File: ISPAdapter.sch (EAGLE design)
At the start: 8 parts, among them U1 SWITCH_IC_QUAD74LVC4066

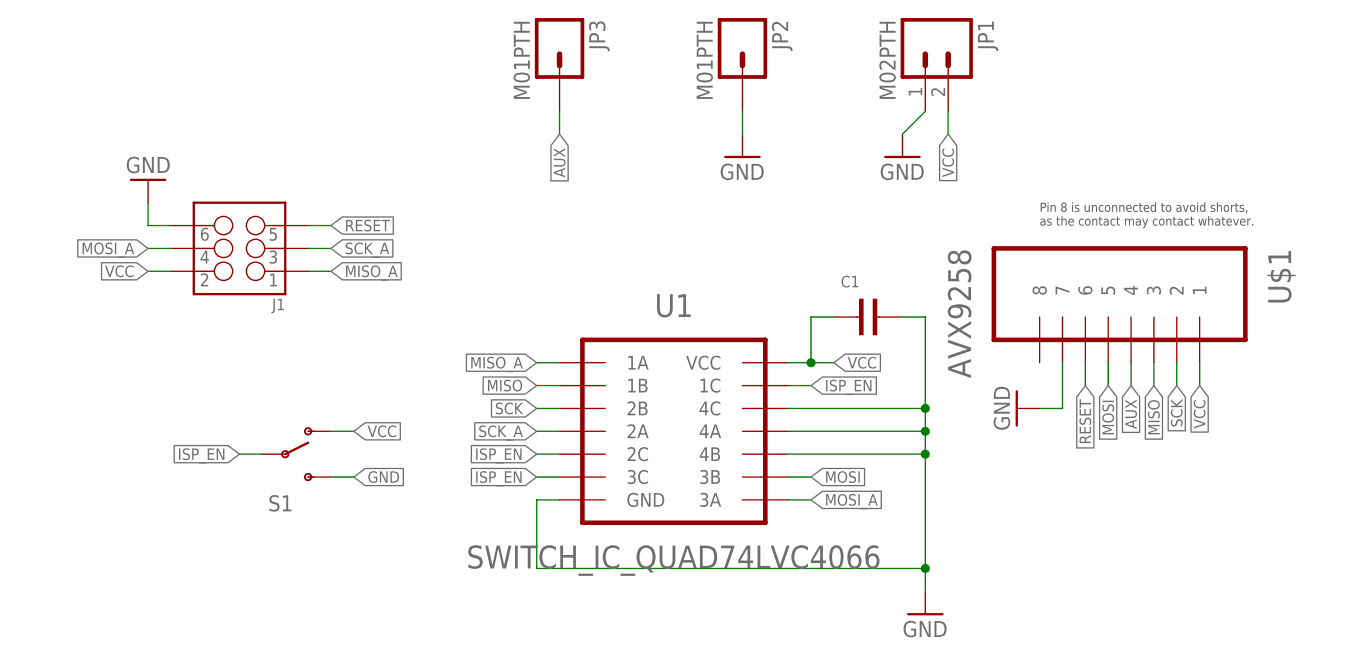
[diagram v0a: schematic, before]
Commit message: Switch IC fitting
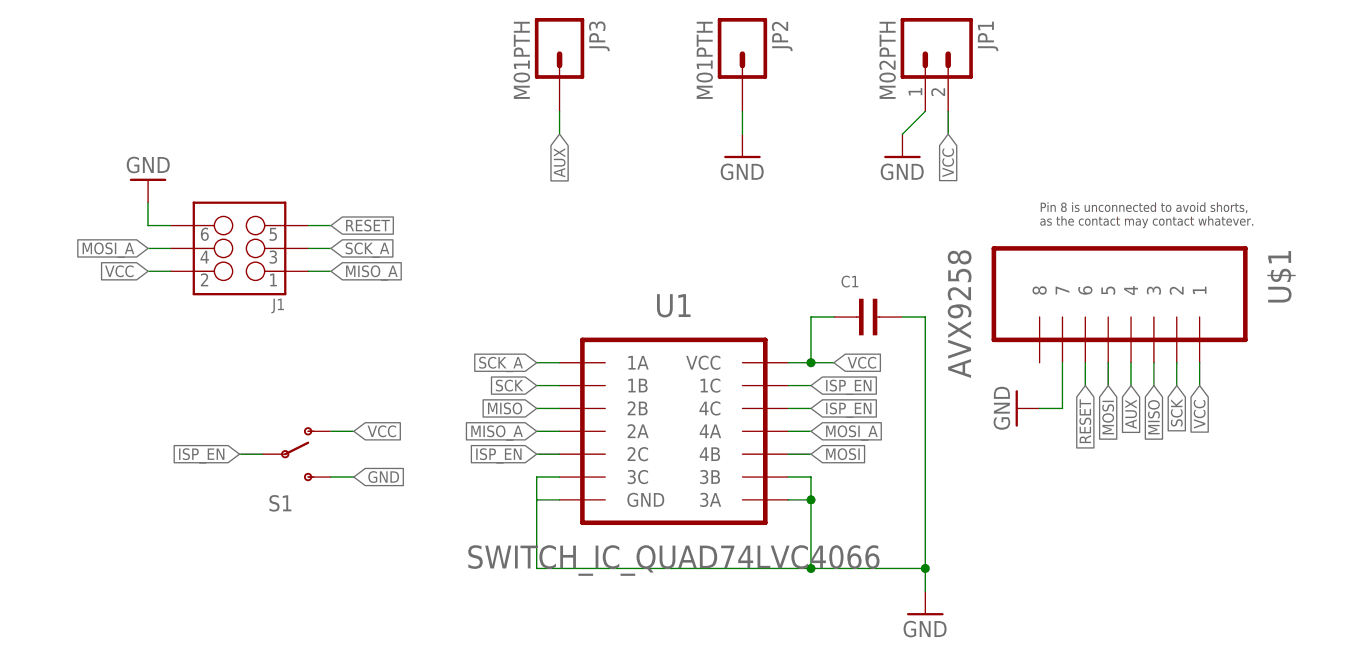
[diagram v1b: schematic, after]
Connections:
- net DGND: now also U1.3A, U1.3B, U1.3C; no longer U1.4A, U1.4B, U1.4C
- net ISP_EN: now also U1.4C; no longer U1.3C
- net MISO: now also U1.2B; no longer U1.1B
- net MISO_A: now also U1.2A; no longer U1.1A
- net MOSI: now also U1.4B; no longer U1.3B
- net MOSI_A: now also U1.4A; no longer U1.3A
- net SCK: now also U1.1B; no longer U1.2B
- net SCK_A: now also U1.1A; no longer U1.2A
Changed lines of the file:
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@@
 </segment>
 <segment>
-<pinref part="U1" gate="G$1" pin="3B"/>
-<wire x1="71.12" y1="43.18" x2="73.66" y2="43.18" width="0.1524" layer="91"/>
-<label x="73.66" y="43.18" size="1.27" layer="95" xref="yes"/>
+<pinref part="U1" gate="G$1" pin="4B"/>
+<wire x1="71.12" y1="45.72" x2="73.66" y2="45.72" width="0.1524" layer="91"/>
+<label x="73.66" y="45.72" size="1.27" layer="95" xref="yes"/>
 </segment>
 </net>
@@
 <pinref part="U1" gate="G$1" pin="GND"/>
 <wire x1="45.72" y1="40.64" x2="43.18" y2="40.64" width="0.1524" layer="91"/>
+<pinref part="U1" gate="G$1" pin="3C"/>
+<wire x1="45.72" y1="43.18" x2="43.18" y2="43.18" width="0.1524" layer="91"/>
+<wire x1="43.18" y1="43.18" x2="43.18" y2="40.64" width="0.1524" layer="91"/>
 </segment>
 <segment>
 <pinref part="GND6" gate="1" pin="GND"/>
 <wire x1="43.18" y1="40.64" x2="43.18" y2="33.02" width="0.1524" layer="91"/>
-<pinref part="U1" gate="G$1" pin="4C"/>
-<wire x1="71.12" y1="50.8" x2="86.36" y2="50.8" width="0.1524" layer="91"/>
-<wire x1="86.36" y1="50.8" x2="86.36" y2="48.26" width="0.1524" layer="91"/>
-<pinref part="U1" gate="G$1" pin="4A"/>
-<wire x1="86.36" y1="48.26" x2="86.36" y2="45.72" width="0.1524" layer="91"/>
-<wire x1="86.36" y1="45.72" x2="86.36" y2="33.02" width="0.1524" layer="91"/>
 <wire x1="86.36" y1="33.02" x2="86.36" y2="30.48" width="0.1524" layer="91"/>
-<wire x1="71.12" y1="48.26" x2="86.36" y2="48.26" width="0.1524" layer="91"/>
-<junction x="86.36" y="48.26"/>
-<pinref part="U1" gate="G$1" pin="4B"/>
-<wire x1="71.12" y1="45.72" x2="86.36" y2="45.72" width="0.1524" layer="91"/>
-<junction x="86.36" y="45.72"/>
-<wire x1="43.18" y1="33.02" x2="86.36" y2="33.02" width="0.1524" layer="91"/>
+<wire x1="43.18" y1="33.02" x2="73.66" y2="33.02" width="0.1524" layer="91"/>
 <junction x="86.36" y="33.02"/>
 <pinref part="C1" gate="G$1" pin="2"/>
+<wire x1="73.66" y1="33.02" x2="86.36" y2="33.02" width="0.1524" layer="91"/>
 <wire x1="83.82" y1="60.96" x2="86.36" y2="60.96" width="0.1524" layer="91"/>
-<wire x1="86.36" y1="60.96" x2="86.36" y2="50.8" width="0.1524" layer="91"/>
-<junction x="86.36" y="50.8"/>
+<wire x1="86.36" y1="60.96" x2="86.36" y2="33.02" width="0.1524" layer="91"/>
+<pinref part="U1" gate="G$1" pin="3B"/>
+<wire x1="71.12" y1="43.18" x2="73.66" y2="43.18" width="0.1524" layer="91"/>
+<pinref part="U1" gate="G$1" pin="3A"/>
+<wire x1="71.12" y1="40.64" x2="73.66" y2="40.64" width="0.1524" layer="91"/>
+<wire x1="73.66" y1="43.18" x2="73.66" y2="40.64" width="0.1524" layer="91"/>
+<wire x1="73.66" y1="40.64" x2="73.66" y2="33.02" width="0.1524" layer="91"/>
+<junction x="73.66" y="40.64"/>
+<junction x="73.66" y="33.02"/>
 </segment>
 </net>
@@
 </segment>
 <segment>
-<pinref part="U1" gate="G$1" pin="1B"/>
-<wire x1="45.72" y1="53.34" x2="43.18" y2="53.34" width="0.1524" layer="91"/>
-<label x="43.18" y="53.34" size="1.27" layer="95" rot="R180" xref="yes"/>
+<pinref part="U1" gate="G$1" pin="2B"/>
+<wire x1="45.72" y1="50.8" x2="43.18" y2="50.8" width="0.1524" layer="91"/>
+<label x="43.18" y="50.8" size="1.27" layer="95" rot="R180" xref="yes"/>
 </segment>
 </net>
@@
 </segment>
 <segment>
-<pinref part="U1" gate="G$1" pin="2B"/>
-<wire x1="45.72" y1="50.8" x2="43.18" y2="50.8" width="0.1524" layer="91"/>
-<label x="43.18" y="50.8" size="1.27" layer="95" rot="R180" xref="yes"/>
+<pinref part="U1" gate="G$1" pin="1B"/>
+<wire x1="45.72" y1="53.34" x2="43.18" y2="53.34" width="0.1524" layer="91"/>
+<label x="43.18" y="53.34" size="1.27" layer="95" rot="R180" xref="yes"/>
 </segment>
 </net>
@@
 </segment>
 <segment>
-<pinref part="U1" gate="G$1" pin="3C"/>
-<wire x1="45.72" y1="43.18" x2="43.18" y2="43.18" width="0.1524" layer="91"/>
-<label x="43.18" y="43.18" size="1.27" layer="95" rot="R180" xref="yes"/>
-</segment>
-<segment>
 <pinref part="S1" gate="1" pin="P"/>
 <wire x1="12.7" y1="45.72" x2="10.16" y2="45.72" width="0.1524" layer="91"/>
 <label x="10.16" y="45.72" size="1.27" layer="95" rot="R180" xref="yes"/>
+</segment>
+<segment>
+<pinref part="U1" gate="G$1" pin="4C"/>
+<wire x1="71.12" y1="50.8" x2="73.66" y2="50.8" width="0.1524" layer="91"/>
+<label x="73.66" y="50.8" size="1.27" layer="95" xref="yes"/>
 </segment>
 </net>
@@
 </segment>
 <segment>
-<pinref part="U1" gate="G$1" pin="2A"/>
-<wire x1="45.72" y1="48.26" x2="43.18" y2="48.26" width="0.1524" layer="91"/>
-<label x="43.18" y="48.26" size="1.27" layer="95" rot="R180" xref="yes"/>
+<pinref part="U1" gate="G$1" pin="1A"/>
+<wire x1="45.72" y1="55.88" x2="43.18" y2="55.88" width="0.1524" layer="91"/>
+<label x="43.18" y="55.88" size="1.27" layer="95" rot="R180" xref="yes"/>
 </segment>
 </net>
@@
 </segment>
 <segment>
-<pinref part="U1" gate="G$1" pin="1A"/>
-<wire x1="45.72" y1="55.88" x2="43.18" y2="55.88" width="0.1524" layer="91"/>
-<label x="43.18" y="55.88" size="1.27" layer="95" rot="R180" xref="yes"/>
+<pinref part="U1" gate="G$1" pin="2A"/>
+<wire x1="45.72" y1="48.26" x2="43.18" y2="48.26" width="0.1524" layer="91"/>
+<label x="43.18" y="48.26" size="1.27" layer="95" rot="R180" xref="yes"/>
 </segment>
 </net>
@@
 </segment>
 <segment>
-<pinref part="U1" gate="G$1" pin="3A"/>
-<wire x1="71.12" y1="40.64" x2="73.66" y2="40.64" width="0.1524" layer="91"/>
-<label x="73.66" y="40.64" size="1.27" layer="95" xref="yes"/>
+<pinref part="U1" gate="G$1" pin="4A"/>
+<wire x1="71.12" y1="48.26" x2="73.66" y2="48.26" width="0.1524" layer="91"/>
+<label x="73.66" y="48.26" size="1.27" layer="95" xref="yes"/>
 </segment>
 </net>

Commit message: Tidy
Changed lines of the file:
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@@
 <instance part="GND3" gate="1" x="83.82" y="78.74"/>
 <instance part="U$1" gate="G$1" x="109.22" y="63.5" rot="R270"/>
-<instance part="GND4" gate="1" x="96.52" y="50.8" rot="R270"/>
+<instance part="GND4" gate="1" x="99.06" y="50.8"/>
 <instance part="JP2" gate="G$1" x="66.04" y="91.44" rot="R270"/>
 <instance part="GND1" gate="1" x="66.04" y="78.74"/>
@@
 <segment>
 <pinref part="GND4" gate="1" pin="GND"/>
-<wire x1="101.6" y1="50.8" x2="99.06" y2="50.8" width="0.1524" layer="91"/>
+<wire x1="101.6" y1="55.88" x2="99.06" y2="53.34" width="0.1524" layer="91"/>
 <pinref part="U$1" gate="G$1" pin="7"/>
-<wire x1="101.6" y1="50.8" x2="101.6" y2="55.88" width="0.1524" layer="91"/>
 </segment>
 <segment>

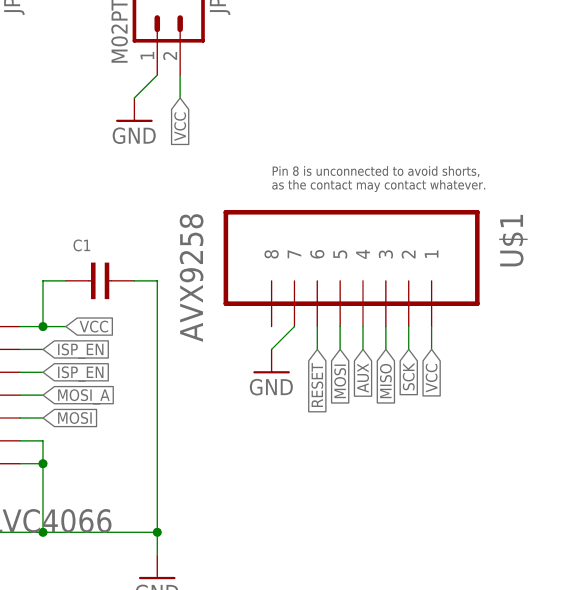
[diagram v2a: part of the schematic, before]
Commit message: Full connector mapping
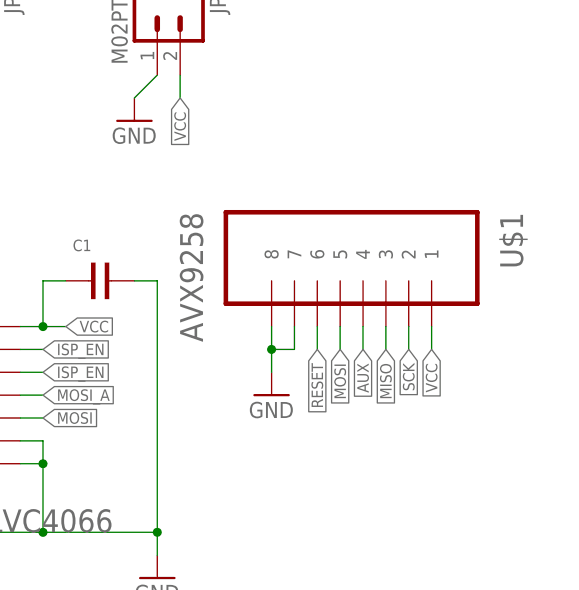
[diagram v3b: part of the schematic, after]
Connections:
- net DGND: now also U$1.8
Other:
- note removed: "Pin 8 is unconnected to avoid shorts, as the contact may contact whatever."
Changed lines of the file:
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@@
 <sheet>
 <plain>
-<text x="99.06" y="73.66" size="1.016" layer="97" align="top-left">Pin 8 is unconnected to avoid shorts,
-as the contact may contact whatever.</text>
 </plain>
 <instances>
@@
 <instance part="GND3" gate="1" x="83.82" y="78.74"/>
 <instance part="U$1" gate="G$1" x="109.22" y="63.5" rot="R270"/>
-<instance part="GND4" gate="1" x="99.06" y="50.8"/>
+<instance part="GND4" gate="1" x="99.06" y="48.26"/>
 <instance part="JP2" gate="G$1" x="66.04" y="91.44" rot="R270"/>
 <instance part="GND1" gate="1" x="66.04" y="78.74"/>
@@
 <segment>
 <pinref part="GND4" gate="1" pin="GND"/>
-<wire x1="101.6" y1="55.88" x2="99.06" y2="53.34" width="0.1524" layer="91"/>
 <pinref part="U$1" gate="G$1" pin="7"/>
+<pinref part="U$1" gate="G$1" pin="8"/>
+<wire x1="99.06" y1="55.88" x2="99.06" y2="53.34" width="0.1524" layer="91"/>
+<wire x1="99.06" y1="53.34" x2="99.06" y2="50.8" width="0.1524" layer="91"/>
+<wire x1="101.6" y1="55.88" x2="101.6" y2="53.34" width="0.1524" layer="91"/>
+<wire x1="101.6" y1="53.34" x2="99.06" y2="53.34" width="0.1524" layer="91"/>
+<junction x="99.06" y="53.34"/>
 </segment>
 <segment>

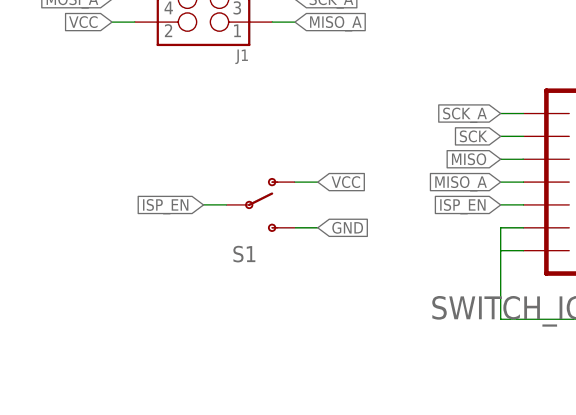
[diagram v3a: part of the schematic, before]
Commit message: Added cap to switch
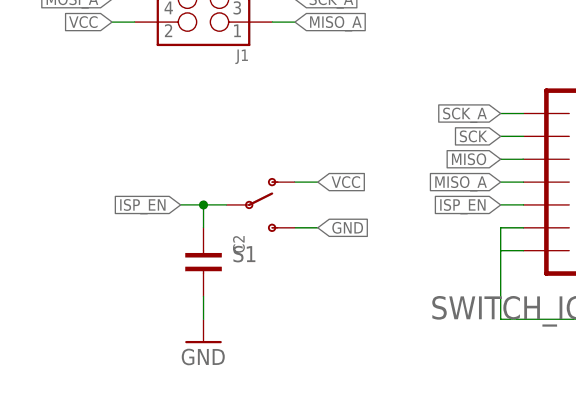
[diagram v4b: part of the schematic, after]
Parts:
- added C2: (no value), dubec:CAP0.1UF_100V
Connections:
- net DGND: now also C2.2
- net ISP_EN: now also C2.1
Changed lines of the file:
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@@
 <part name="GND6" library="SparkFun-Aesthetics" deviceset="GND" device=""/>
 <part name="C1" library="dubec" deviceset="CAP" device="4.7UF_10V"/>
+<part name="C2" library="dubec" deviceset="CAP" device="0.1UF_100V"/>
+<part name="GND5" library="SparkFun-Aesthetics" deviceset="GND" device=""/>
 </parts>
 <sheets>
@@
 <instance part="GND6" gate="1" x="86.36" y="27.94"/>
 <instance part="C1" gate="G$1" x="78.74" y="60.96"/>
+<instance part="C2" gate="G$1" x="10.16" y="40.64" rot="R270"/>
+<instance part="GND5" gate="1" x="10.16" y="30.48"/>
 </instances>
 <busses>
@@
 <junction x="73.66" y="33.02"/>
 </segment>
+<segment>
+<pinref part="GND5" gate="1" pin="GND"/>
+<wire x1="10.16" y1="35.56" x2="10.16" y2="33.02" width="0.1524" layer="91"/>
+<pinref part="C2" gate="G$1" pin="2"/>
+</segment>
 </net>
 <net name="MISO" class="0">
@@
 <pinref part="S1" gate="1" pin="P"/>
 <wire x1="12.7" y1="45.72" x2="10.16" y2="45.72" width="0.1524" layer="91"/>
-<label x="10.16" y="45.72" size="1.27" layer="95" rot="R180" xref="yes"/>
-</segment>
-<segment>
+<label x="7.62" y="45.72" size="1.27" layer="95" rot="R180" xref="yes"/>
+<pinref part="C2" gate="G$1" pin="1"/>
+<wire x1="10.16" y1="45.72" x2="7.62" y2="45.72" width="0.1524" layer="91"/>
+<wire x1="10.16" y1="45.72" x2="10.16" y2="43.18" width="0.1524" layer="91"/>
+<junction x="10.16" y="45.72"/>
+</segment>
+<segment>
